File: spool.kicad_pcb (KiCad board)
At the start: 4 copper layers, 80 x 87 mm, 116 parts, among them J1 USB_B_Micro, J10 Switch_1, J11 Switch_1, J12 Conn_02x10_Counter_Clockwise, J13 Conn_02x10_Counter_Clockwise, J2 SWD, J3 Switch_1, J4 Switch_1, J5 Switch_1, J6 Switch_2, J7 Conn_01x02, J8 Conn_01x08, J9 Conn_01x05, M1 Motor_DC, Q1 AO3400A, Q2 2N7002, SW1 USB_BOOT, SW2 RESET, SW3 SW_Push_DPDT, SW4 SW_Coded_SH-7010, SW5 SW_Push_DPDT, U1 TPS63070RNMR, U10 HT75xx-1-SOT89, U11 TPL0401B-10-Q1, U12 BS612, U14 PCF8563T, U2 RPI-441C1, U3 AS5600-ASOT, U4 RPI-441C1, U5 RPI-441C1, U6 DRV8871DDA, U7 W25Q128JVS, U8 RP2040, U9 BS612, Y1 Crystal_GND24, Y2 Crystal

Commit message: WIP
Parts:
- removed J10, J11: Switch_1, Connector_PinHeader_2.54mm:PinHeader_1x02_P2.54mm_Vertical
- removed J12: Conn_02x10_Counter_Clockwise, Connector_PinHeader_2.54mm:PinHeader_2x10_P2.54mm_Vertical
- removed J9: Conn_01x05, Connector_PinHeader_2.54mm:PinHeader_1x05_P2.54mm_Vertical
- removed R13: 1k, Resistor_SMD:R_0603_1608Metric
- added C33: 100n, Capacitor_SMD:C_0402_1005Metric, F.Cu at (-0.83, -33.1)
- added C34: 100uF, Capacitor_SMD:CP_Elec_6.3x7.7, F.Cu at (-7.12, -30.5)
- added C35: 100uF, Capacitor_SMD:CP_Elec_6.3x7.7, F.Cu at (-14.2, -30.5)
- added D10: D, Diode_SMD:D_SOD-323_HandSoldering, F.Cu at (9.62, -24.4)
- added D11: D, Diode_SMD:D_SOD-323_HandSoldering, F.Cu at (26.6, 42.6)
- added D4: D, Diode_SMD:D_SOD-323_HandSoldering, F.Cu at (7.58, -28.4)
- added D5: D, Diode_SMD:D_SOD-323_HandSoldering, F.Cu at (11.5, -28.5)
- added D6: D, Diode_SMD:D_SOD-323_HandSoldering, F.Cu at (10.4, 2.78)
- added D7: D, Diode_SMD:D_SOD-323_HandSoldering, F.Cu at (7.59, -24.4)
- added D8: D, Diode_SMD:D_SOD-323_HandSoldering, F.Cu at (5.68, -24.4)
- added D9: D, Diode_SMD:D_SOD-323_HandSoldering, F.Cu at (11.5, -24.4)
- added J14: Conn_01x07, Connector_PinHeader_2.54mm:PinHeader_1x07_P2.54mm_Vertical, F.Cu at (-29.4, 28.9)
- added R33: 47k, Resistor_SMD:R_0805_2012Metric_Pad1.20x1.40mm_HandSolder, F.Cu at (9.03, -31.9)
- BZ1: footprint cacophony-library:BUZ-TH_BD9.0-P5.00-D0.6-FD -> cacophony-library:BUZ-TH_BD9.0-P4.00-D0.6-FD
- H1, H2, H3, H4: footprint cacophony-library:MountingHole_3.2mm_M3 -> cacophony-library:MountingHole_3.5mm_M3
- J13: footprint Connector_PinHeader_2.54mm:PinHeader_2x10_P2.54mm_Vertical -> cacophony-library:test-headers
- L1: value INDUCTOR -> 1.5H
- R10, R12: value 1k -> 100k; footprint Resistor_SMD:R_0603_1608Metric -> Resistor_SMD:R_0402_1005Metric
- R11, R5, R8: value 1k -> 47Ω
- R15: value R -> 47k
- R6, R7, R9: value 1k -> 10k; footprint Resistor_SMD:R_0603_1608Metric -> Resistor_SMD:R_0402_1005Metric
- moved M1 62.0 mm to (-18.4, -37.9), turned to 180 degrees
- moved R15 57.5 mm to (3.25, -34.2), turned to 0 degrees
- moved U6 57.4 mm to (0.89, -29.9)
- moved R9 56.6 mm to (-27.7, 18.0), turned to 90 degrees
- moved R12 50.1 mm to (4.08, -25.1), turned to -90 degrees
- moved R10 43.2 mm to (13.6, -27.1), turned to 0 degrees
- moved Q1 34.4 mm to (13.4, 0.21), turned to 0 degrees
- moved R14 30.2 mm to (11.0, -0.25), turned to -90 degrees
- moved SW2 21.0 mm to (-20.5, 19.1)
- moved SW1 14.5 mm to (-2.70, 47.4), turned to 180 degrees
- moved J2 13.5 mm to (-21.3, 24.2), turned to 90 degrees
- moved SW4 11.7 mm to (19.0, 36.7)
- moved J8 11.5 mm to (-13.8, 41.2)
- moved R28 11.0 mm to (-5.77, -13.3), turned to 0 degrees
- moved BZ1 10.7 mm to (30.2, 48.1), turned to -90 degrees
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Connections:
- J13 pad 10: unconnected-(J13-Pin_10-Pad10) -> PIN_10
- J13 pad 12: unconnected-(J13-Pin_12-Pad12) -> PIN_12
- J13 pad 14: unconnected-(J13-Pin_14-Pad14) -> PIN_14
- J13 pad 16: unconnected-(J13-Pin_16-Pad16) -> PIN_16
- J13 pad 18: unconnected-(J13-Pin_18-Pad18) -> PIN_18
- J13 pad 2: unconnected-(J13-Pin_2-Pad2) -> PIN_2
- J13 pad 20: unconnected-(J13-Pin_20-Pad20) -> PIN_20
- J13 pad 4: unconnected-(J13-Pin_4-Pad4) -> PIN_4
- J13 pad 6: unconnected-(J13-Pin_6-Pad6) -> PIN_6
- J13 pad 8: unconnected-(J13-Pin_8-Pad8) -> PIN_8
- R10 pad 1: /PHOTO_2_OUT_PHY -> Net-(D10-K)
- R12 pad 1: /PHOTO_3_OUT_PHY -> Net-(D4-A)
- R12 pad 2: PHOTO_3_OUT -> GND
- R6 pad 1: /PHOTO_1_OUT_PHY -> +3V3
- R6 pad 2: PHOTO_1_OUT -> PHOTO_HOME_OUT
- R7 pad 1: /PHOTO_1_OUT_PHY -> +3V3
- R7 pad 2: GND -> PHOTO_RELEASE_OUT
- R9 pad 1: /PHOTO_2_OUT_PHY -> +3V3
- R9 pad 2: PHOTO_2_OUT -> PHOTO_RESET_OUT
- U2 pad 3: +3V3 -> PHOTO_HOME_OUT
- U2 pad 4: /PHOTO_1_OUT_PHY -> GND
- U4 pad 3: +3V3 -> PHOTO_RELEASE_OUT
- U4 pad 4: /PHOTO_2_OUT_PHY -> GND
- U5 pad 3: +3V3 -> PHOTO_RESET_OUT
- U5 pad 4: /PHOTO_3_OUT_PHY -> GND
- U6 pad 2: H_IN2 -> Net-(D4-A)
- U6 pad 3: H_IN1 -> Net-(D10-K)
- U8 pad 11: R_ENC_1 -> SWITCH_2
- U8 pad 12: GPIO_9 -> H_IN1
- U8 pad 13: GPIO_10 -> H_IN2
- U8 pad 14: GPIO_11 -> Net-(D6-A)
- U8 pad 17: PHOTO_2_OUT -> PHOTO_RELEASE_OUT
- U8 pad 18: PHOTO_1_OUT -> PHOTO_HOME_OUT
- U8 pad 29: EN_PHOTO -> PHOTO_RESET_OUT
- U8 pad 30: PHOTO_3_OUT -> GPIO_19
- U8 pad 31: H_IN1 -> GPIO_20
- U8 pad 32: H_IN2 -> GPIO_21
- U8 pad 36: RP2040_TX_IN -> RP2040_TX_OUT
- U8 pad 37: RP2040_RX_IN -> RP2040_RX_OUT
- U8 pad 40: RP2040_TX_OUT -> RP2040_TX_IN
- U8 pad 41: RP2040_RX_OUT -> RP2040_RX_IN
- U8 pad 5: SWITCH_1 -> R_ENC_4
- U8 pad 6: SWITCH_2 -> R_ENC_2
- U8 pad 7: R_ENC_2 -> R_ENC_1
- U8 pad 8: R_ENC_4 -> R_ENC_8
- U8 pad 9: R_ENC_8 -> SWITCH_1
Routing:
- net PHOTO_RESET_OUT: track 0.00 -> 89.0 mm, vias 0 -> 3
- net PHOTO_RELEASE_OUT: track 0.00 -> 87.0 mm, vias 0 -> 1
- net PHOTO_HOME_OUT: track 0.00 -> 53.3 mm
- net H_IN2: track 12.2 -> 62.7 mm, vias 0 -> 2
- net H_IN1: track 12.6 -> 62.4 mm, vias 0 -> 2
- net PHOTO_1_OUT: track 45.2 -> 0.00 mm
- net +12V: track 125.9 -> 162.0 mm, vias 0 -> 18
- net PHOTO_2_OUT: track 35.7 -> 0.00 mm
- net Net-(D6-A): track 0.00 -> 28.7 mm, vias 0 -> 2
- net +3V3_Lin: track 84.4 -> 58.2 mm, vias 4 -> 3
- net GPIO_9: track 24.5 -> 0.00 mm
- net Net-(M1--): track 6.76 -> 30.4 mm
- net PHOTO_3_OUT: track 23.5 -> 0.00 mm
- net GPIO_10: track 22.8 -> 0.00 mm
- net GPIO_11: track 22.5 -> 0.00 mm
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- added copper zone on In2.Cu, net +12V
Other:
- board size 80 x 87 mm -> 80 x 95 mm
- board text added: "12V"
- board text added: "3V3"
- board text added: "CCW"
- board text added: "CW"
- board text added: "Cacophony Spool Controller ${TAG}"
- board text added: "RX_IN"
- board text added: "RX_OUT"
- board text added: "TX_IN"
- board text added: "TX_OUT"
- board text removed: "CLK"
- board text removed: "SWD"

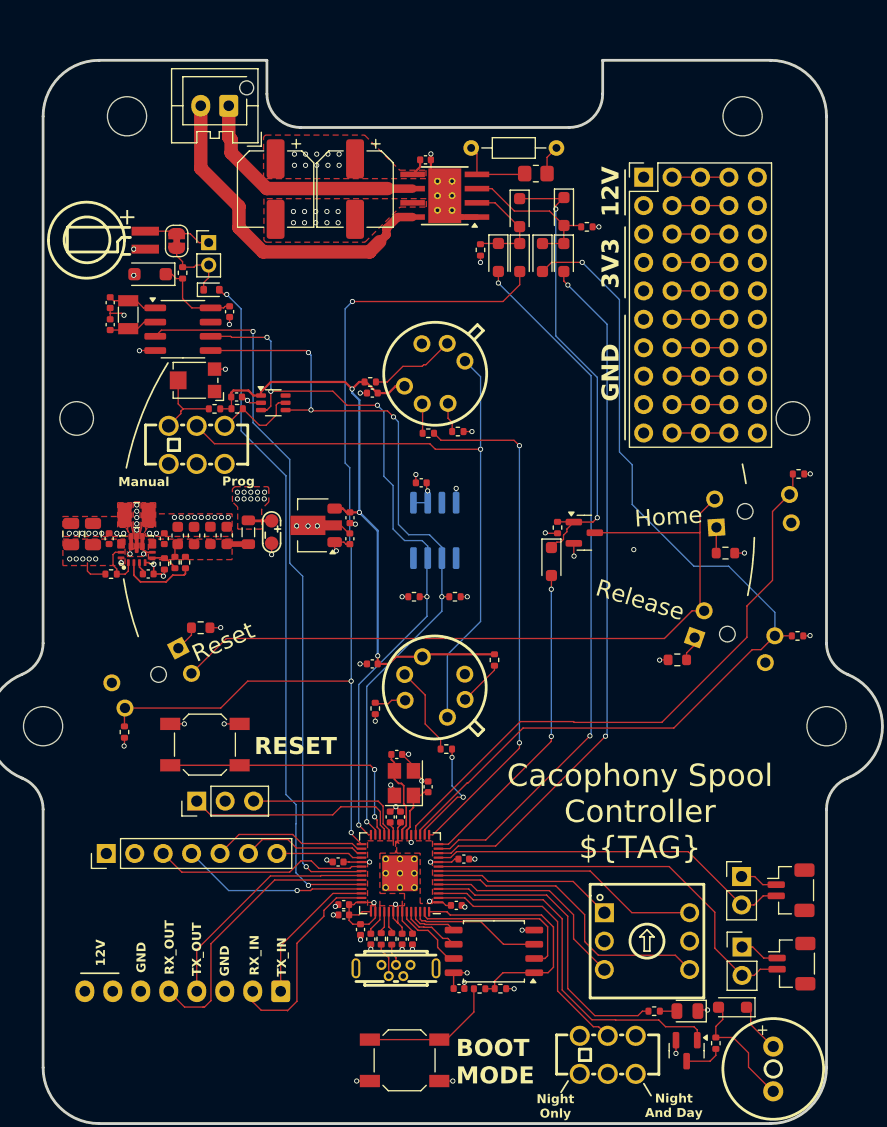
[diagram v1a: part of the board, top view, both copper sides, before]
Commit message: Add changes for magnet release
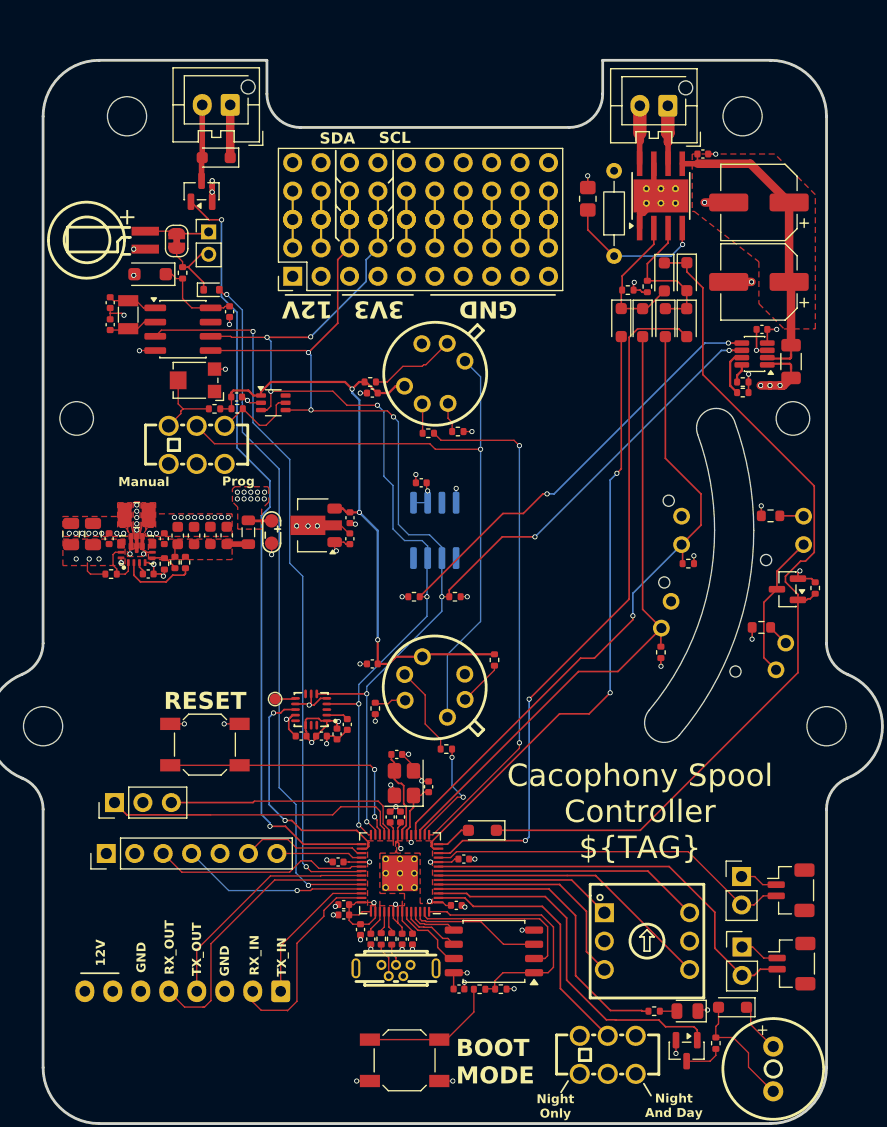
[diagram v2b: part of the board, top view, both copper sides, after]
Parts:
- removed R11, R5, R8: 47Ω, Resistor_SMD:R_0603_1608Metric
- removed R9: 10k, Resistor_SMD:R_0402_1005Metric
- removed U2, U4, U5: RPI-441C1, cacophony-library:OPTO-TH_RPI-441C1
- added C101: 100n, Capacitor_SMD:C_0402_1005Metric, F.Cu at (-8.74, 18.2)
- added C102: 100n, Capacitor_SMD:C_0402_1005Metric, F.Cu at (-7.82, 17.3)
- added C103: 2.2uF, Capacitor_SMD:C_0402_1005Metric, F.Cu at (-10.1, 18.4)
- added C104: 100n, Capacitor_SMD:C_0402_1005Metric, F.Cu at (29.2, -18.0)
- added C105: 2.2uF, Capacitor_SMD:C_0402_1005Metric, F.Cu at (-11.9, 18.4)
- added D101: D, Diode_SMD:D_SOD-323_HandSoldering, F.Cu at (-19.5, -33.3)
- added L101: ElectromagneticActor, Connector_JST:JST_XA_B02B-XASK-1-A_1x02_P2.50mm_Vertical, F.Cu at (-18.3, -38.0)
- added Q101: Q_NMOS_GSD, Package_TO_SOT_SMD:SOT-23, F.Cu at (-20.8, -30.3)
- added R101: 100k, Resistor_SMD:R_0402_1005Metric, F.Cu at (27.5, -12.3)
- added R102: 100k, Resistor_SMD:R_0402_1005Metric, F.Cu at (27.5, -13.3)
- added R103: R_Shunt, cacophony-library:R_1206_Shunt, F.Cu at (31.8, -15.1)
- added R104: 150Ω, Resistor_SMD:R_0603_1608Metric, F.Cu at (30.0, -1.30)
- added R105: 150Ω, Resistor_SMD:R_0603_1608Metric, F.Cu at (29.2, 8.67)
- added TP101: TestPoint, cacophony-library:TP_PAD, F.Cu at (-14.3, 15.1)
- added U101: MMA8451QR1, cacophony-library:QFN-16_L3.0-W3.0-P0.50-TL_FXOS8700CQR1, F.Cu at (-11.0, 16.0)
- added U102: INA219AxDCN, Package_TO_SOT_SMD:SOT-23-8, F.Cu at (28.6, -15.8)
- added U103: DY-ITR8402, cacophony-library:OPTO-TH_DY-ITR8402, B.Cu at (25.8, 9.40)
- added U104: DY-ITR8402, cacophony-library:OPTO-TH_DY-ITR8402, B.Cu at (27.5, 0.00)
- R33: value 47k -> 33k
- U7: footprint Package_SO:SOIC-8_5.23x5.23mm_P1.27mm -> Package_SO:SOIC-8_5.3x5.3mm_P1.27mm
- moved C35 43.2 mm to (29.0, -29.3), turned to 180 degrees
- moved M1 39.2 mm to (20.8, -37.9)
- moved C34 37.0 mm to (29.0, -22.2), turned to 180 degrees
- moved J13 32.6 mm to (-12.7, -22.7), turned to 90 degrees
- moved D6 24.8 mm to (4.25, 26.8), turned to 180 degrees
- moved C33 24.8 mm to (23.9, -33.6)
- moved R14 23.7 mm to (34.0, 5.15), turned to 90 degrees
- moved U6 19.3 mm to (20.2, -29.9), turned to 90 degrees
- moved Q1 18.8 mm to (31.5, 5.26), turned to 180 degrees
- moved R15 16.0 mm to (16.0, -24.5), turned to 90 degrees
- moved D4 14.1 mm to (20.5, -22.6)
- moved R12 13.7 mm to (17.2, -21.5), turned to 0 degrees
- moved R6 12.7 mm to (22.6, 2.97)
- moved D10 12.4 mm to (20.6, -18.6)
- moved D9 12.4 mm to (22.5, -18.6)
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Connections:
- C33 pad 1: +12V -> /h_bridge_vcc
- C34 pad 1: +12V -> /h_bridge_vcc
- C35 pad 1: +12V -> /h_bridge_vcc
- D10 pad 2: PHOTO_RELEASE_OUT -> PHOTO_HOME_OUT
- J13 pad 10: PIN_10 -> unconnected-(J13-Pin_10-Pad10)_2
- J13 pad 12: PIN_12 -> unconnected-(J13-Pin_12-Pad12)_1
- J13 pad 14: PIN_14 -> unconnected-(J13-Pin_14-Pad14)_2
- J13 pad 16: PIN_16 -> unconnected-(J13-Pin_16-Pad16)
- J13 pad 18: PIN_18 -> unconnected-(J13-Pin_18-Pad18)
- J13 pad 2: PIN_2 -> unconnected-(J13-Pin_2-Pad2)_2
- J13 pad 20: PIN_20 -> unconnected-(J13-Pin_20-Pad20)
- J13 pad 4: PIN_4 -> unconnected-(J13-Pin_4-Pad4)
- J13 pad 6: PIN_6 -> SDA
- J13 pad 8: PIN_8 -> SCL
- J14 pad 5: GPIO_19 -> unconnected-(J14-Pin_5-Pad5)
- R7 pad 2: PHOTO_RELEASE_OUT -> PHOTO_RESET_OUT
- U6 pad 5: +12V -> /h_bridge_vcc
- U8 pad 17: PHOTO_RELEASE_OUT -> PHOTO_RESET_OUT
- U8 pad 29: PHOTO_RESET_OUT -> RELEASE
- U8 pad 30: GPIO_19 -> Accel INT1
- U8 pad 6: R_ENC_2 -> R_ENC_1
- U8 pad 7: R_ENC_1 -> R_ENC_2
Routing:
- net +12V: track 162.0 -> 27.4 mm, vias 18 -> 9
- net PHOTO_RELEASE_OUT: track 87.0 -> 0.00 mm, vias 1 -> 0
- net RELEASE: track 0.00 -> 68.9 mm, vias 0 -> 2
- net SCL: track 67.3 -> 122.7 mm, vias 5 -> 9
- net PHOTO_CATHODE: track 67.7 -> 13.1 mm
- net SDA: track 67.9 -> 118.9 mm, vias 5 -> 8
- net EN_PHOTO: track 41.3 -> 79.7 mm, vias 2 -> 0
- net PHOTO_RESET_OUT: track 89.0 -> 57.9 mm, vias 3 -> 0
- net Net-(D6-A): track 28.7 -> 3.18 mm, vias 2 -> 0
- net Net-(M1--): track 30.4 -> 5.19 mm
- net /h_bridge_vcc: track 0.00 -> 24.7 mm
- net GND: track 55.5 -> 80.0 mm, vias 82 -> 79
- net Accel INT1: track 0.00 -> 21.8 mm, vias 0 -> 2
- net +3V3: track 43.9 -> 61.3 mm, vias 27 -> 29
- net Net-(M1-+): track 21.8 -> 5.19 mm
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- added copper zone on F.Cu, net /h_bridge_vcc
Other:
- outline, holes or cut-outs redrawn
- board text added: "20°"
- board text added: "SCL"
- board text added: "SDA"
- board text removed: "Home"
- board text removed: "Release"
- board text removed: "Reset"
